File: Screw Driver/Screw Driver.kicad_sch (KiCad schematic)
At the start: 33 parts, among them J1 V_Main, J2 Conn_01x05_Pin, Q1 NVMFS5C628NLET1G, U1 AP63205WU, U2 VNH5019A-E

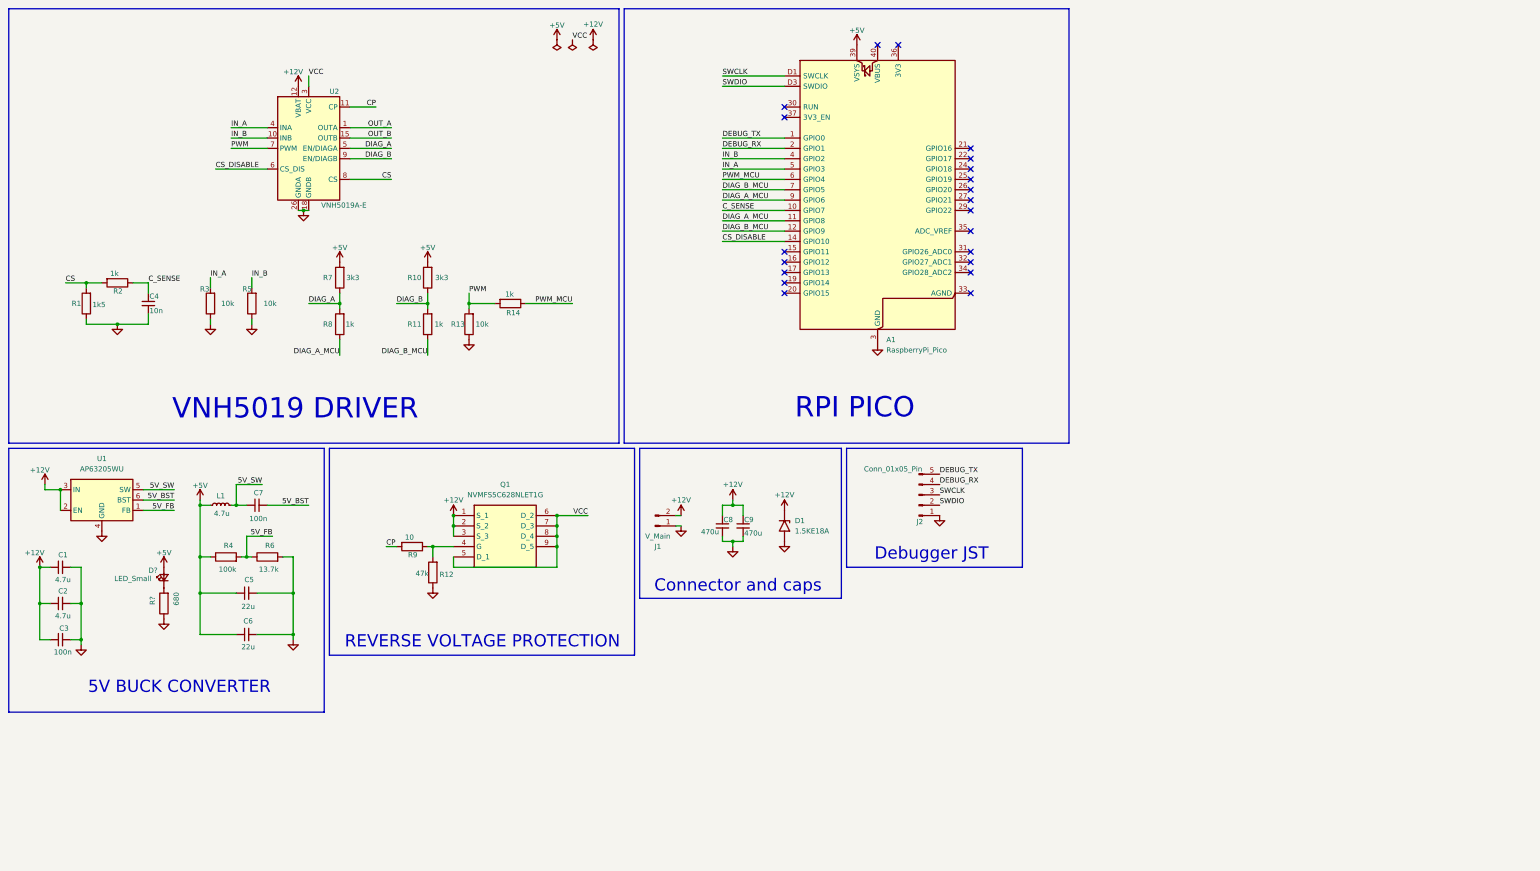
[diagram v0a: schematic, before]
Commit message: Added essentials, tentative PCB layout
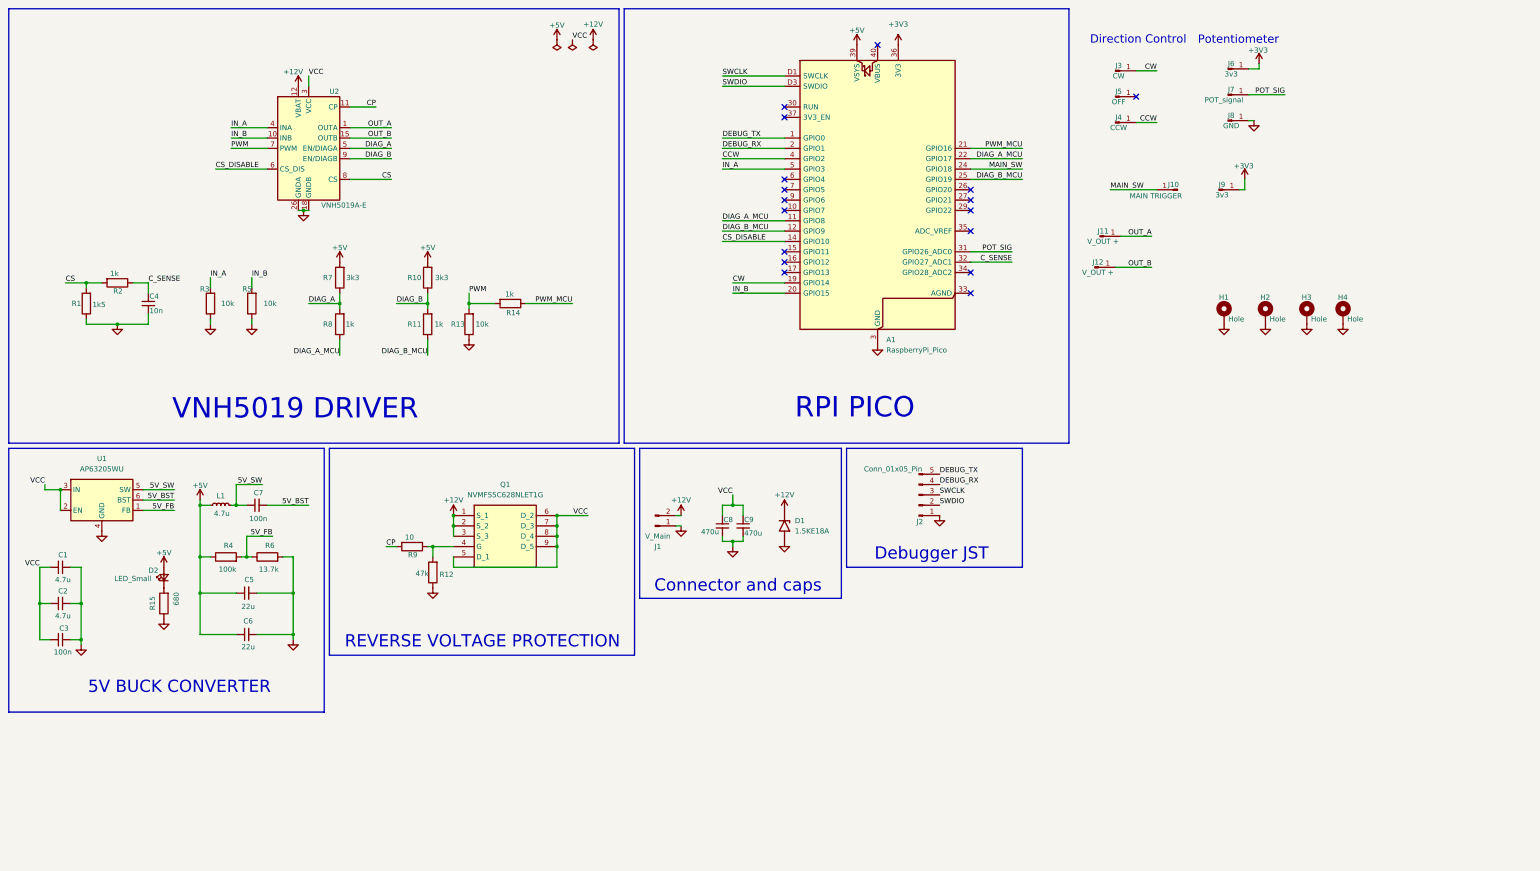
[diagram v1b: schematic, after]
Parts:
- added H1, H2, H3, H4: Hole, MountingHole:MountingHole_3.2mm_M3_Pad, symbol Mechanical:MountingHole_Pad
- added J10: MAIN TRIGGER, Connector_PinHeader_2.54mm:PinHeader_1x01_P2.54mm_Vertical, symbol Connector:Conn_01x01_Pin
- added J11, J12: V_OUT +, Solder_Pads:Solder_Pad_10x10mm_withVias, symbol Connector:Conn_01x01_Pin
- added J3: CW, Connector_PinHeader_2.54mm:PinHeader_1x01_P2.54mm_Vertical, symbol Connector:Conn_01x01_Pin
- added J4: CCW, Connector_PinHeader_2.54mm:PinHeader_1x01_P2.54mm_Vertical, symbol Connector:Conn_01x01_Pin
- added J5: OFF, Connector_PinHeader_2.54mm:PinHeader_1x01_P2.54mm_Vertical, symbol Connector:Conn_01x01_Pin
- added J6, J9: 3v3, Connector_PinHeader_2.54mm:PinHeader_1x01_P2.54mm_Vertical, symbol Connector:Conn_01x01_Pin
- added J7: POT_signal, Connector_PinHeader_2.54mm:PinHeader_1x01_P2.54mm_Vertical, symbol Connector:Conn_01x01_Pin
- added J8: GND, Connector_PinHeader_2.54mm:PinHeader_1x01_P2.54mm_Vertical, symbol Connector:Conn_01x01_Pin
- D2: renamed from D?; footprint (none) -> LED_SMD:LED_0603_1608Metric_Pad1.05x0.95mm_HandSolder
- Q1: footprint Mosfet:NVMFS5C442NLWFAFT1G -> Package_SO:ONSemi_SO-8FL_488AA
- gave numbers to parts that had none: 1
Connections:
- net +12V: no longer C1.1, C2.1, C3.1, C8.1, C9.1, U1.2 (EN), U1.3 (IN)
- net C_SENSE: now also A1.32 (GPIO27_ADC1); no longer A1.10 (GPIO7)
- net DIAG_A_MCU: now also A1.22 (GPIO17); no longer A1.9 (GPIO6)
- net DIAG_B_MCU: now also A1.25 (GPIO19); no longer A1.7 (GPIO5)
- net GND: now also H1.1, H2.1, H3.1, H4.1, J8.1 (Pin_1)
- net IN_B: now also A1.20 (GPIO15); no longer A1.4 (GPIO2)
- net OUT_A: now also J11.1 (Pin_1)
- net OUT_B: now also J12.1 (Pin_1)
- net PWM_MCU: now also A1.21 (GPIO16); no longer A1.6 (GPIO4)
- net VCC: now also C1.1, C2.1, C3.1, C8.1, C9.1, U1.2 (EN), U1.3 (IN)
- net CW: now reaches A1.19 (GPIO14)
- net CW: now also J3.1 (Pin_1)
- net MAIN_SW: now reaches A1.24 (GPIO18)
- net MAIN_SW: now also J10.1 (Pin_1)
- net POT_SIG: now reaches A1.31 (GPIO26_ADC0)
- net POT_SIG: now also J7.1 (Pin_1)
- net +3V3: now reaches A1.36 (3V3)
- net +3V3: now also J6.1 (Pin_1), J9.1 (Pin_1)
- new net CCW: A1.4 (GPIO2), J4.1 (Pin_1)
- no-connect marks 21 -> 17
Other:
- note added: "Direction Control"
- note added: "Potentiometer"

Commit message: Some routing done
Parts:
- C4: footprint Resistor_SMD:R_0603_1608Metric_Pad0.98x0.95mm_HandSolder -> Capacitor_SMD:C_0603_1608Metric_Pad1.08x0.95mm_HandSolder
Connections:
- net CCW: now also A1.16 (GPIO12); no longer A1.4 (GPIO2)
- net CW: now also A1.17 (GPIO13); no longer A1.19 (GPIO14)
- net DIAG_A_MCU: no longer A1.11 (GPIO8)
- net DIAG_B_MCU: no longer A1.12 (GPIO9)
- net GND: now also J5.1 (Pin_1)
- net IN_A: now also A1.26 (GPIO20); no longer A1.5 (GPIO3)
- net IN_B: now also A1.19 (GPIO14); no longer A1.20 (GPIO15)
- net MAIN_SW: now also A1.12 (GPIO9); no longer A1.24 (GPIO18)
- no-connect marks 17 -> 18
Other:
- moved on the sheet: J11, J12

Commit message: Some more routing done
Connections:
- net C_SENSE: now also A1.31 (GPIO26_ADC0); no longer A1.32 (GPIO27_ADC1)
- net POT_SIG: now also A1.32 (GPIO27_ADC1); no longer A1.31 (GPIO26_ADC0)

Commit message: Routing fully done
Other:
- moved on the sheet: A1, C1, C2, C3, C4, C5, C6, C7, C8, C9, D1, D2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

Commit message: Improved Layout
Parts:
- Q1: MFP (none) -> NTMFS2D5N08XT1G; Manufacturer_Part_Number NTMFS2D5N08XT1G -> (none)
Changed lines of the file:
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@@
+			)
+		)
+		(property "MFP" ""
+			(at 161.29 175.26 0)
+			(effects
+				(font
+					(size 1.27 1.27)
+				)
+				(hide yes)
 			)
 		)
@@
 			)
 		)
-		(property "Manufacturer_Part_Number" "NTMFS2D5N08XT1G"
+		(property "MFP" "NTMFS2D5N08XT1G"
 			(at 273.05 981.61 0)
 			(effects
